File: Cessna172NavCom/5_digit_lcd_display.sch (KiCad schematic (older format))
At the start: 2 parts, among them U1 MAX7219 COM standby, U2 3651A

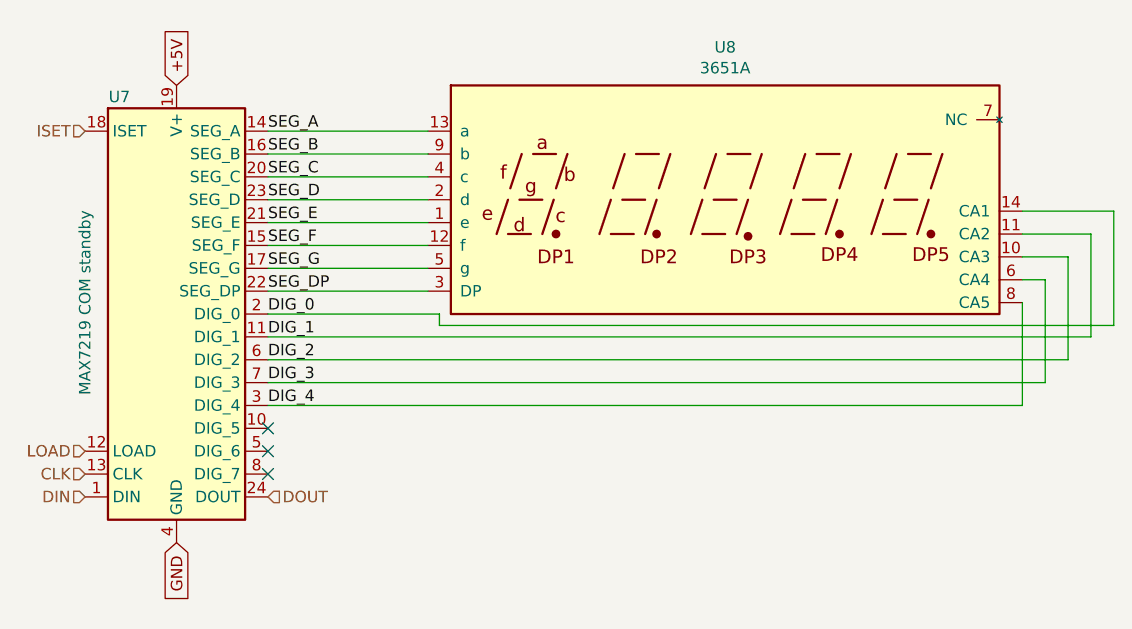
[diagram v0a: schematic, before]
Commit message: Merge connector mapping
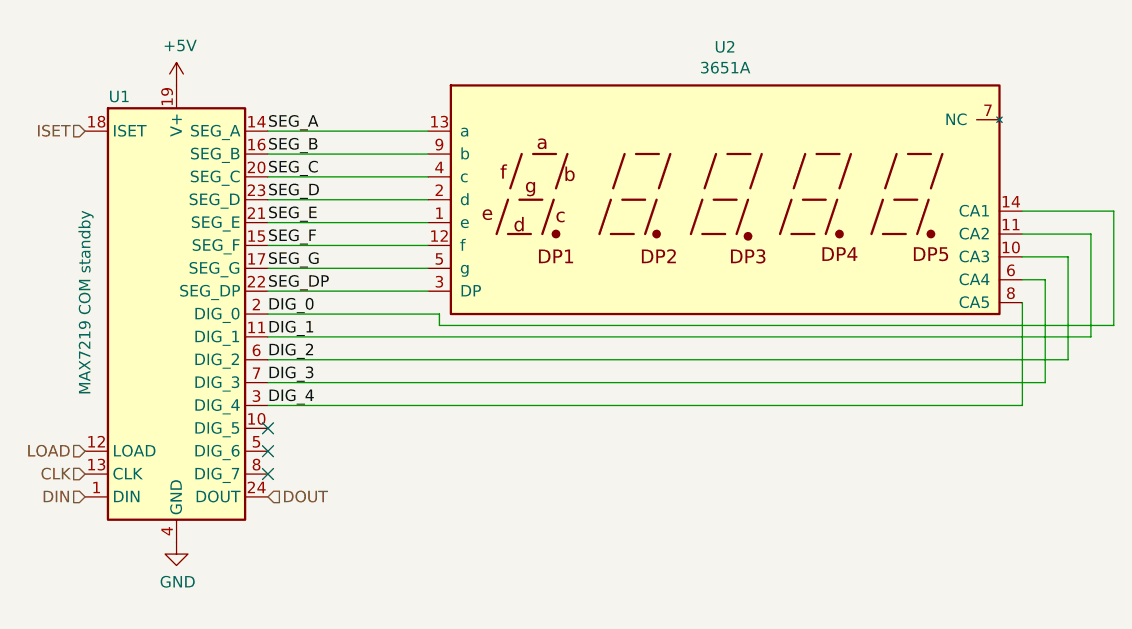
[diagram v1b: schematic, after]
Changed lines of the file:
@@
 $Descr A4 11693 8268
 encoding utf-8
-Sheet 4 15
+Sheet 2 15
 Title ""
 Date ""
@@
 AR Path="/5F68A9EB/5F60E2D2" Ref="U13"  Part="1"
 AR Path="/5F68A9F8/5F60E2D2" Ref="U15"  Part="1"
-F 0 "U7" H 2500 5000 50  0000 C CNN
+F 0 "U1" H 2500 5000 50  0000 C CNN
 F 1 "MAX7219 COM standby" V 2350 4100 50  0000 C CNN
 F 2 "Package_SO:SSOP-24_3.9x8.7mm_P0.635mm" H 2700 4100 50  0001 C CNN
@@
 NoConn ~ 3150 4650
 NoConn ~ 3150 4750
-Text GLabel 2750 3050 1    50   Input ~ 0
-+5V
-Text GLabel 2750 5050 3    50   Input ~ 0
-GND
 Text Label 3150 3250 0    50   ~ 0
 SEG_A
@@
 AR Path="/5F68A9EB/5F5F5D43" Ref="U14"  Part="1"
 AR Path="/5F68A9F8/5F5F5D43" Ref="U16"  Part="1"
-F 0 "U8" H 5150 4217 50  0000 C CNN
+F 0 "U2" H 5150 4217 50  0000 C CNN
 F 1 "3651A" H 5150 4126 50  0000 C CNN
 F 2 "Cessna 172 nav and com radio:3651A" H 4950 3550 50  0001 C CNN
@@
 Wire Wire Line
 	6850 3600 6850 4100
+$Comp
+L power:+5V #PWR0121
+U 1 1 5F693DF9
+P 2750 3050
+AR Path="/5F60A880/5F693DF9" Ref="#PWR0121"  Part="1"
+AR Path="/5F613967/5F693DF9" Ref="#PWR0123"  Part="1"
+AR Path="/5F613974/5F693DF9" Ref="#PWR0125"  Part="1"
+AR Path="/5F61163D/5F693DF9" Ref="#PWR0142"  Part="1"
+AR Path="/5F68A9CC/5F693DF9" Ref="#PWR0144"  Part="1"
+AR Path="/5F68A9DF/5F693DF9" Ref="#PWR0146"  Part="1"
+AR Path="/5F68A9EB/5F693DF9" Ref="#PWR0148"  Part="1"
+AR Path="/5F68A9F8/5F693DF9" Ref="#PWR0150"  Part="1"
+F 0 "#PWR0150" H 2750 2900 50  0001 C CNN
+F 1 "+5V" H 2765 3223 50  0000 C CNN
+F 2 "" H 2750 3050 50  0001 C CNN
+F 3 "" H 2750 3050 50  0001 C CNN
+	1    2750 3050
+	1    0    0    -1
+$EndComp
+$Comp
+L power:GND #PWR0122
+U 1 1 5F693FE6
+P 2750 5050
+AR Path="/5F60A880/5F693FE6" Ref="#PWR0122"  Part="1"
+AR Path="/5F613967/5F693FE6" Ref="#PWR0124"  Part="1"
+AR Path="/5F613974/5F693FE6" Ref="#PWR0126"  Part="1"
+AR Path="/5F61163D/5F693FE6" Ref="#PWR0143"  Part="1"
+AR Path="/5F68A9CC/5F693FE6" Ref="#PWR0145"  Part="1"
+AR Path="/5F68A9DF/5F693FE6" Ref="#PWR0147"  Part="1"
+AR Path="/5F68A9EB/5F693FE6" Ref="#PWR0149"  Part="1"
+AR Path="/5F68A9F8/5F693FE6" Ref="#PWR0151"  Part="1"
+F 0 "#PWR0151" H 2750 4800 50  0001 C CNN
+F 1 "GND" H 2755 4877 50  0000 C CNN
+F 2 "" H 2750 5050 50  0001 C CNN
+F 3 "" H 2750 5050 50  0001 C CNN
+	1    2750 5050
+	1    0    0    -1
+$EndComp
 $EndSCHEMATC

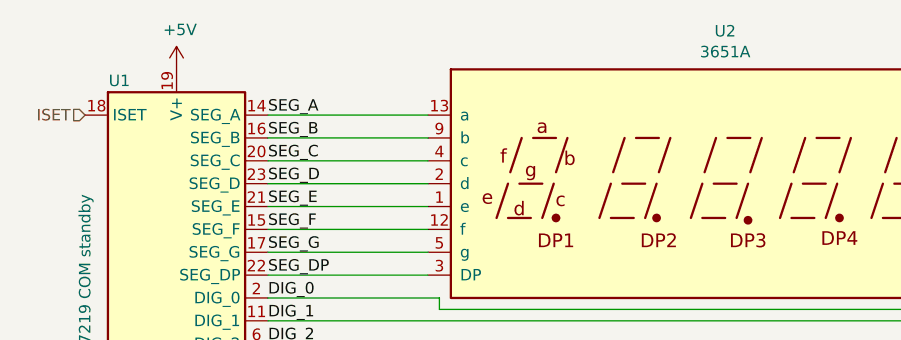
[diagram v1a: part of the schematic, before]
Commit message: Fix courtyard overlap for routing
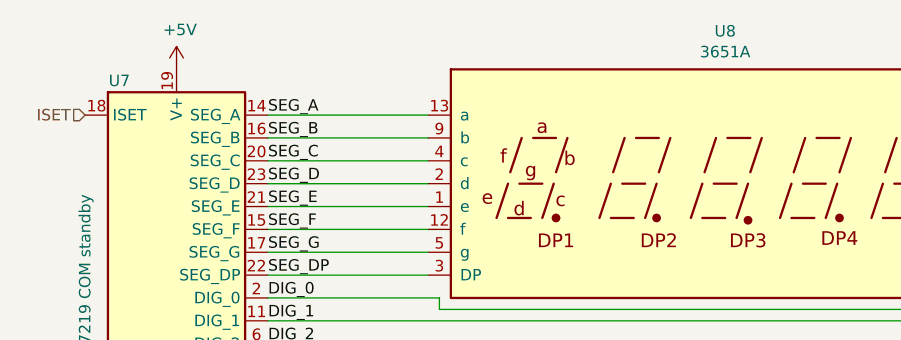
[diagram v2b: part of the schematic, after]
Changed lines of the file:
@@
 $Descr A4 11693 8268
 encoding utf-8
-Sheet 2 15
+Sheet 4 15
 Title ""
 Date ""
@@
 AR Path="/5F68A9EB/5F60E2D2" Ref="U13"  Part="1"
 AR Path="/5F68A9F8/5F60E2D2" Ref="U15"  Part="1"
-F 0 "U1" H 2500 5000 50  0000 C CNN
+F 0 "U7" H 2500 5000 50  0000 C CNN
 F 1 "MAX7219 COM standby" V 2350 4100 50  0000 C CNN
 F 2 "Package_SO:SSOP-24_3.9x8.7mm_P0.635mm" H 2700 4100 50  0001 C CNN
@@
 AR Path="/5F68A9EB/5F5F5D43" Ref="U14"  Part="1"
 AR Path="/5F68A9F8/5F5F5D43" Ref="U16"  Part="1"
-F 0 "U2" H 5150 4217 50  0000 C CNN
+F 0 "U8" H 5150 4217 50  0000 C CNN
 F 1 "3651A" H 5150 4126 50  0000 C CNN
 F 2 "Cessna 172 nav and com radio:3651A" H 4950 3550 50  0001 C CNN

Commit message: Remove unnecessary items, rename some of the nets
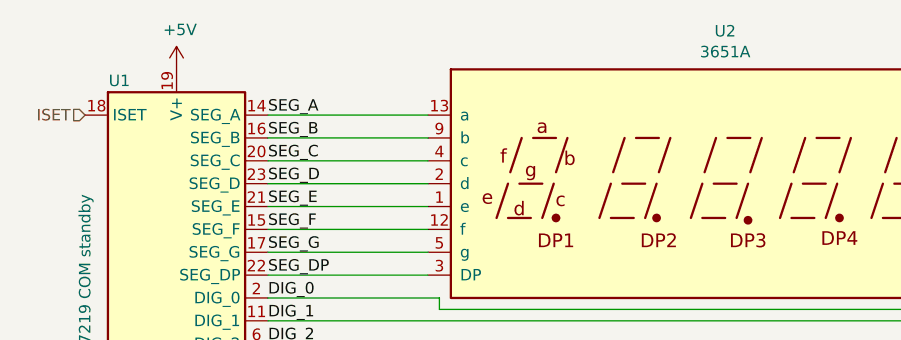
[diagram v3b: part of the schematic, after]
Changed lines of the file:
@@
 $Descr A4 11693 8268
 encoding utf-8
-Sheet 4 15
+Sheet 2 13
 Title ""
 Date ""
@@
 AR Path="/5F68A9EB/5F60E2D2" Ref="U13"  Part="1"
 AR Path="/5F68A9F8/5F60E2D2" Ref="U15"  Part="1"
-F 0 "U7" H 2500 5000 50  0000 C CNN
+F 0 "U1" H 2500 5000 50  0000 C CNN
 F 1 "MAX7219 COM standby" V 2350 4100 50  0000 C CNN
 F 2 "Package_SO:SSOP-24_3.9x8.7mm_P0.635mm" H 2700 4100 50  0001 C CNN
@@
 AR Path="/5F68A9EB/5F5F5D43" Ref="U14"  Part="1"
 AR Path="/5F68A9F8/5F5F5D43" Ref="U16"  Part="1"
-F 0 "U8" H 5150 4217 50  0000 C CNN
+F 0 "U2" H 5150 4217 50  0000 C CNN
 F 1 "3651A" H 5150 4126 50  0000 C CNN
 F 2 "Cessna 172 nav and com radio:3651A" H 4950 3550 50  0001 C CNN
@@
 AR Path="/5F68A9EB/5F693DF9" Ref="#PWR0148"  Part="1"
 AR Path="/5F68A9F8/5F693DF9" Ref="#PWR0150"  Part="1"
-F 0 "#PWR0150" H 2750 2900 50  0001 C CNN
+F 0 "#PWR0121" H 2750 2900 50  0001 C CNN
 F 1 "+5V" H 2765 3223 50  0000 C CNN
 F 2 "" H 2750 3050 50  0001 C CNN
@@
 AR Path="/5F68A9EB/5F693FE6" Ref="#PWR0149"  Part="1"
 AR Path="/5F68A9F8/5F693FE6" Ref="#PWR0151"  Part="1"
-F 0 "#PWR0151" H 2750 4800 50  0001 C CNN
+F 0 "#PWR0122" H 2750 4800 50  0001 C CNN
 F 1 "GND" H 2755 4877 50  0000 C CNN
 F 2 "" H 2750 5050 50  0001 C CNN
